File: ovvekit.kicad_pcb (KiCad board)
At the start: 4 copper layers, 76 x 76 mm, 102 parts, among them IC1 MAX4466EXK+T, J1 ESP_PROG_JTAG, J2 ESP_PROG_UART, J201 Power_Planes, Q201 Q_PMOS_GSD, SW1 SW_Push, SW2 SW_Push, SW3 SW_Push, U1 ESP32-WROOM-32

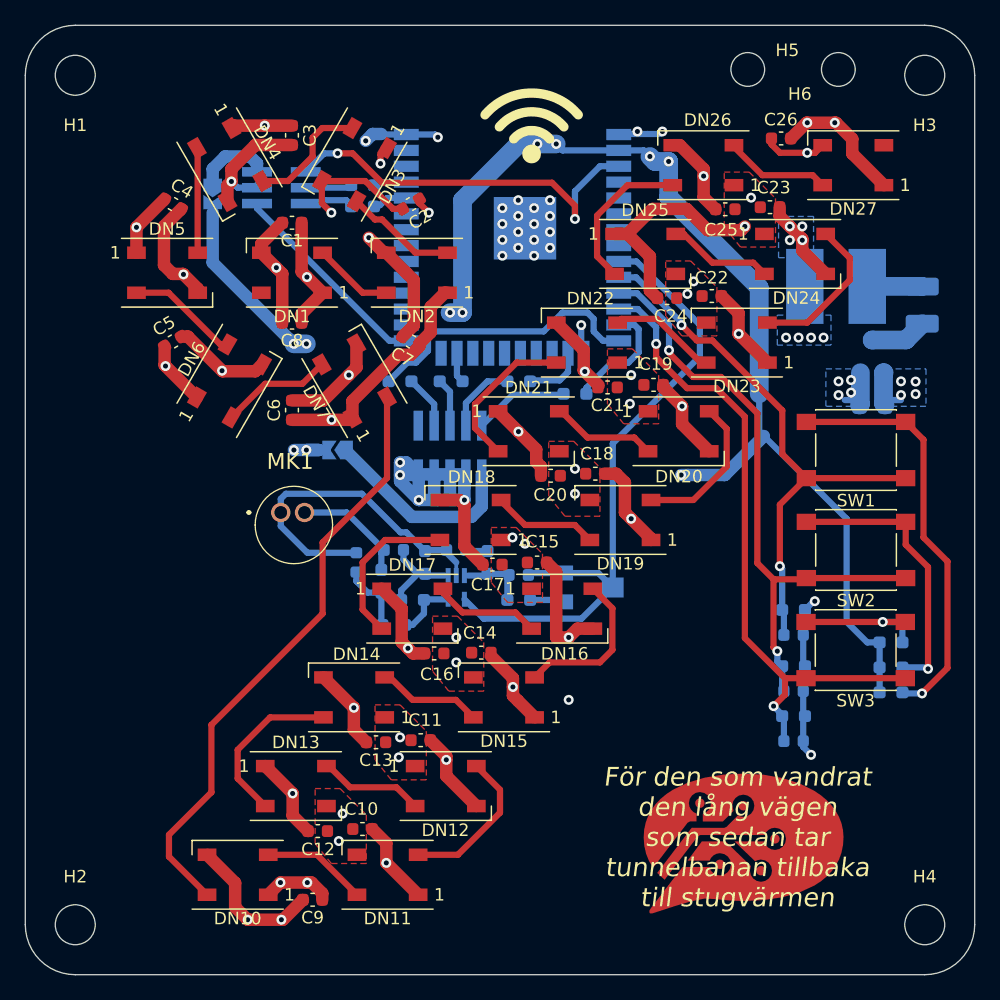
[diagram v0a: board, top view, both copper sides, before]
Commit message: Changed board size to Y is centered.
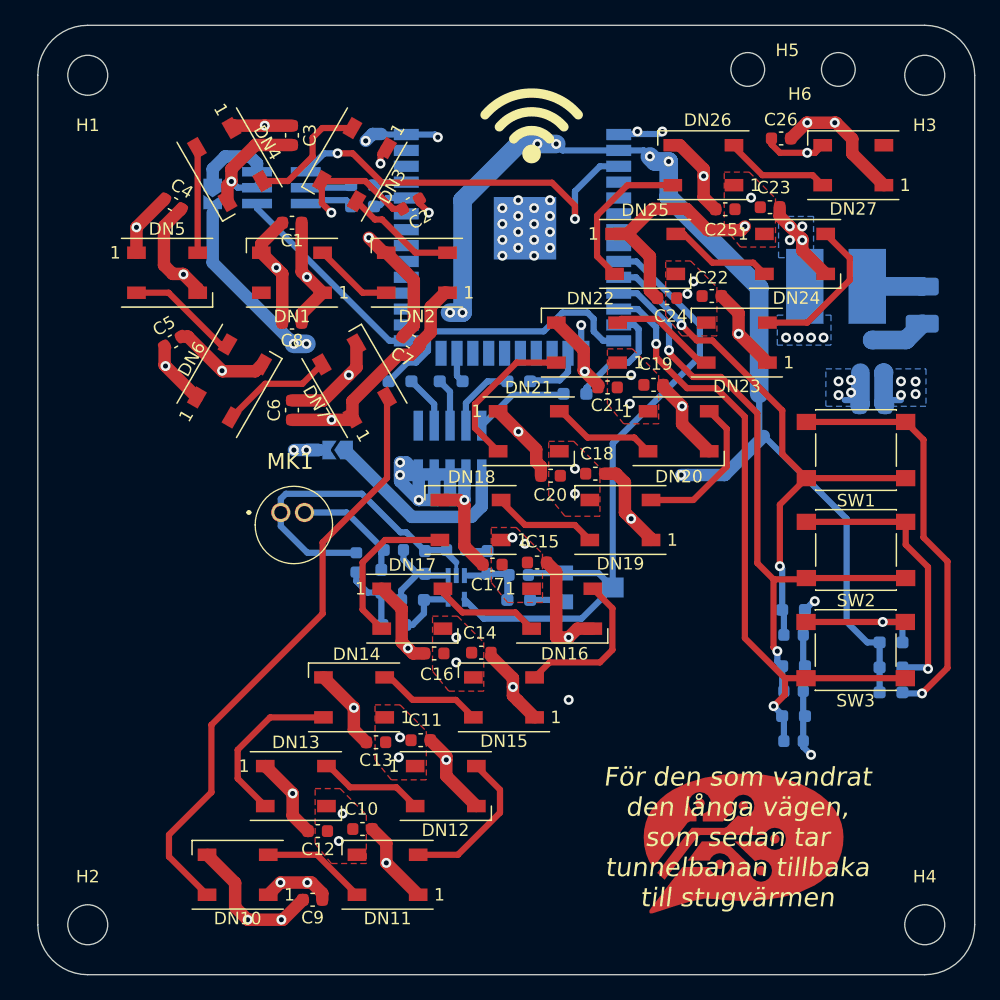
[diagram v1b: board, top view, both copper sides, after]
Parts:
- moved H1 1.00 mm to (-22.0, -3.00)
- moved H2 1.00 mm to (-22.0, 65.0)
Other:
- board size 76 x 76 mm -> 75 x 76 mm
- board text added: "För den som vandrat den långa vägen, som sedan tar tunnelbanan tillbaka till stugvärmen"
- board text removed: "För den som vandrat den lång vägen som sedan tar tunnelbanan tillbaka till stugvärmen"
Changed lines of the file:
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@@
   )
   (module MountingHole:MountingHole_3.2mm_M3_ISO7380 (layer F.Cu)
-    (at -23 65)
+    (at -22 65)
     (descr "Mounting Hole 3.2mm, no annular, M3, ISO7380")
     (tags "mounting hole 3.2mm no annular m3 iso7380")
@@
   )
   (module MountingHole:MountingHole_3.2mm_M3_ISO7380 (layer F.Cu)
-    (at -23 -3)
+    (at -22 -3)
     (descr "Mounting Hole 3.2mm, no annular, M3, ISO7380")
     (tags "mounting hole 3.2mm no annular m3 iso7380")
@@
     )
   )
-  (gr_text "För den som vandrat \nden lång vägen \nsom sedan tar \ntunnelbanan tillbaka \ntill stugvärmen\n" (at 30 58) (layer F.SilkS)
+  (gr_text "För den som vandrat \nden långa vägen, \nsom sedan tar \ntunnelbanan tillbaka \ntill stugvärmen\n" (at 30 58) (layer F.SilkS)
     (effects (font (size 1.5 1.5) (thickness 0.3) italic))
   )
-  (gr_line (start -23 69) (end 45 69) (layer Edge.Cuts) (width 0.05))
-  (gr_arc (start -23 -3) (end -23 -7) (angle -90) (layer Edge.Cuts) (width 0.05))
+  (gr_line (start -22 69) (end 45 69) (layer Edge.Cuts) (width 0.05))
+  (gr_arc (start -22 -3) (end -22 -7) (angle -90) (layer Edge.Cuts) (width 0.05))
   (gr_arc (start 45 -3) (end 49 -3) (angle -90) (layer Edge.Cuts) (width 0.05))
   (gr_arc (start 45 65) (end 45 69) (angle -90) (layer Edge.Cuts) (width 0.05))
-  (gr_arc (start -23 65) (end -27 65) (angle -90) (layer Edge.Cuts) (width 0.05))
-  (gr_line (start -27 65) (end -27 -3) (layer Edge.Cuts) (width 0.05))
+  (gr_arc (start -22 65) (end -26 65) (angle -90) (layer Edge.Cuts) (width 0.05))
+  (gr_line (start -26 65) (end -26 -3) (layer Edge.Cuts) (width 0.05))
   (gr_line (start 49 -3) (end 49 65) (layer Edge.Cuts) (width 0.05))
-  (gr_line (start -23 -7) (end 45 -7) (layer Edge.Cuts) (width 0.05))
+  (gr_line (start -22 -7) (end 45 -7) (layer Edge.Cuts) (width 0.05))
   (segment (start 6.285 19.255) (end 6.184999 19.355001) (width 0.5) (layer B.Cu) (net 0) (status 30))
   (segment (start -0.002137 14.406545) (end -3.202137 11.206545) (width 0.5) (layer F.Cu) (net 1) (status 20))

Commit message: Changed so mic is in local library.
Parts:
- MK1: footprint SamacSys_Parts:CMEJ062742P -> Special_Parts:CMEJ062742P
